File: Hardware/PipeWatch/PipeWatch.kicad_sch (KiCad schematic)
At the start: 19 parts, among them J1 WJ126V-5.0-2P, J3 UART, J4 JTAG, U1 IRM-10-5_C20618064, U3 ESP32-S3-WROOM-1-N16R8, U5 XIAO-ESP32-S3-DIP

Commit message: tweeked the Layout
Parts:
- removed C4: 10n, Capacitor_SMD:C_0603_1608Metric, symbol Device:C
- removed R8: R_Photo, OptoDevice:R_LDR_5.0x4.1mm_P3mm_Vertical, symbol Device:R_Photo
- removed R9: 10M, Resistor_SMD:R_0603_1608Metric, symbol Device:R
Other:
- added sheet PhotowiederstandInnen (Photowiederstand.kicad_sch)

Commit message: Started implementing the accelerometer
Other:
- added sheet MSU (MSU.kicad_sch)
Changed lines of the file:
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@@
+	)
+	(sheet
+		(at 55.88 143.51)
+		(size 12.7 8.89)
+		(exclude_from_sim no)
+		(in_bom yes)
+		(on_board yes)
+		(dnp no)
+		(fields_autoplaced yes)
+		(stroke
+			(width 0.1524)
+			(type solid)
+		)
+		(fill
+			(color 0 0 0 0.0000)
+		)
+		(property "Sheetname" "MSU"
+			(at 55.88 142.7984 0)
+			(effects
+				(font
+					(size 1.27 1.27)
+				)
+				(justify left bottom)
+			)
+		)
+		(property "Sheetfile" "MSU.kicad_sch"
+			(at 55.88 152.9846 0)
+			(effects
+				(font
+					(size 1.27 1.27)
+				)
+				(justify left top)
+			)
+		)
+		(instances
+			(project "PipeWatch"
+				(path "/149975cd-655c-40c3-be76-7a7ba16694c7"
+					(page "5")
+				)
+			)
+		)
 	)
 	(sheet

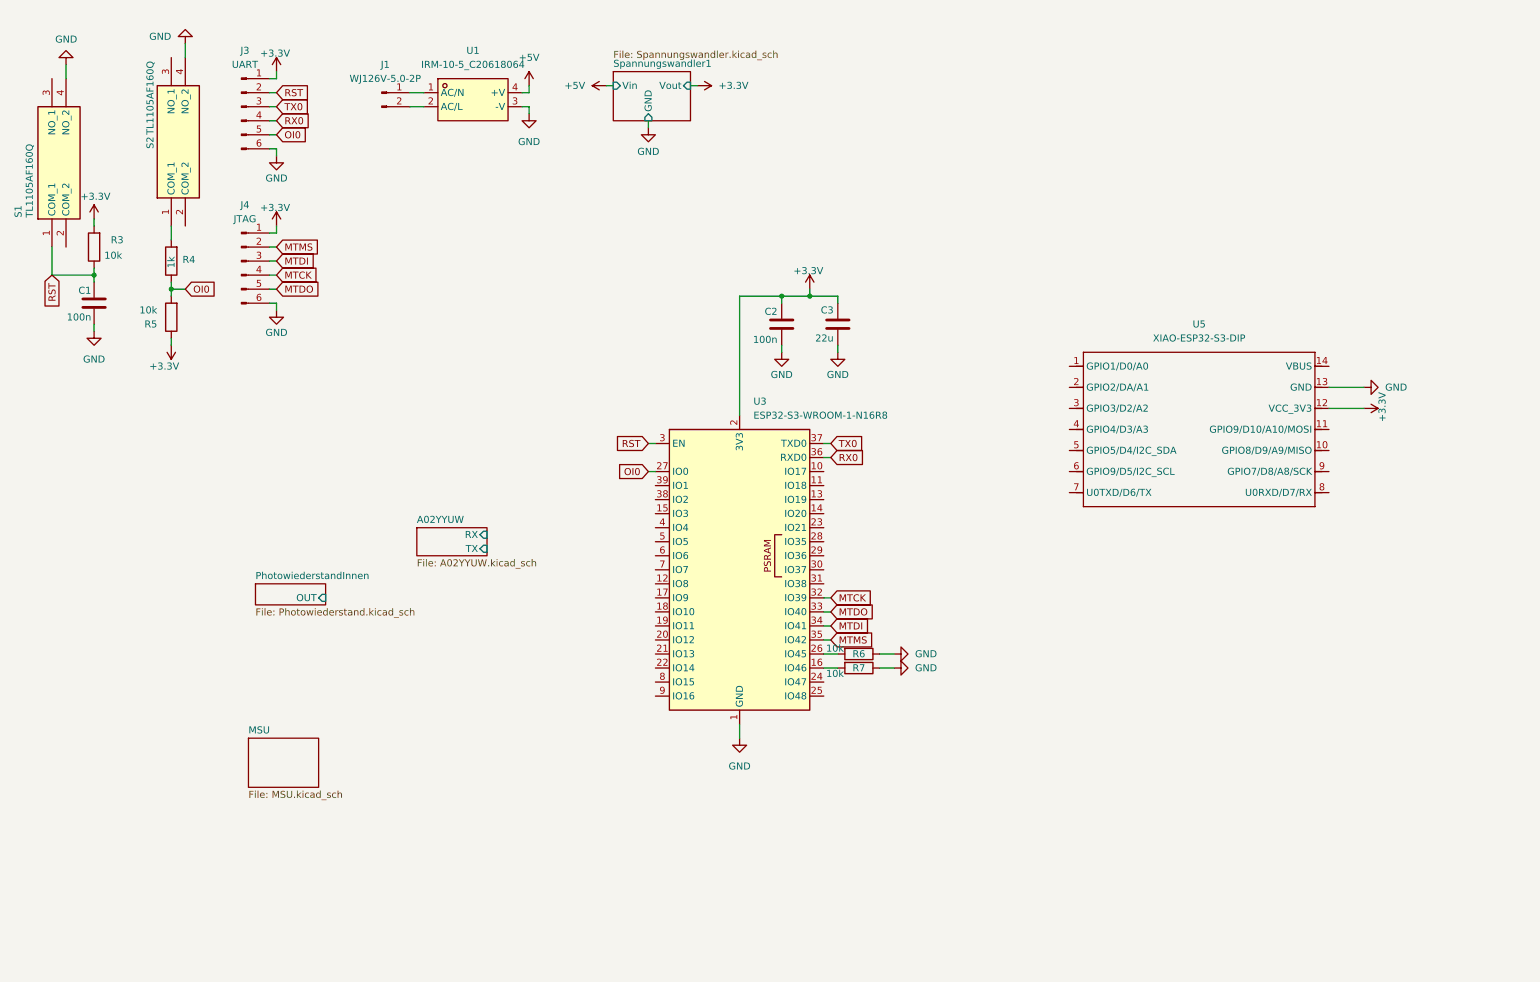
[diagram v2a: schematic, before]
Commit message: added Binky parts and a load of 3d references
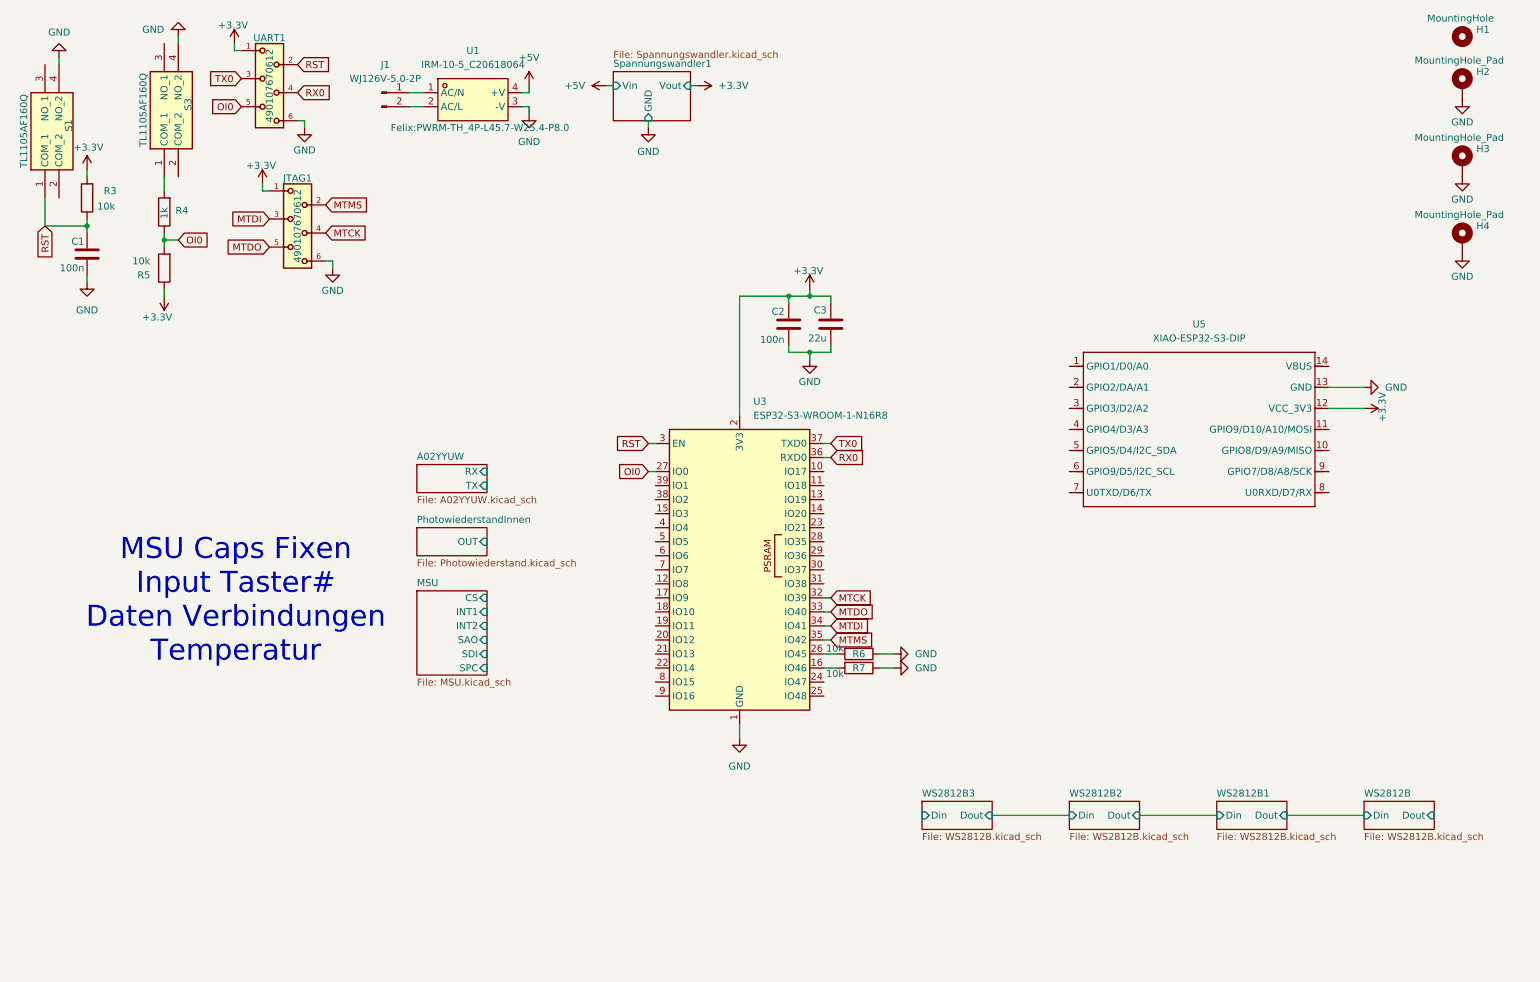
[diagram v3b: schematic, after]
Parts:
- removed J3: UART, Felix_ProgHeader:490107670612, symbol Connector:Conn_01x06_Pin
- removed J4: JTAG, Felix_ProgHeader:490107670612, symbol Connector:Conn_01x06_Pin
- removed S1, S2: TL1105AF160Q, Library:TL1105AF160Q, symbol TL1105AF160Q:TL1105AF160Q
- added H1: MountingHole, MountingHole:MountingHole_3.2mm_M3, symbol Mechanical:MountingHole
- added H2, H3, H4: MountingHole_Pad, MountingHole:MountingHole_3.2mm_M3_DIN965_Pad_TopBottom, symbol Mechanical:MountingHole_Pad
- added JTAG1, UART1: 490107670612, Felix_Connectors:490107670612, symbol Felix_Connectors:490107670612
- added S1, S3: TL1105AF160Q, Felix:TL1105AF160Q, symbol Felix:TL1105AF160Q
- J1: footprint Felix:CONN-TH_WJ126V-5.0-2P -> Felix_Connectors:CONN-TH_WJ126V-5.0-2P
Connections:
- net +3.3V: now also JTAG1.1, UART1.1
- net GND: now also H2.1, H3.1, H4.1, JTAG1.6, S1.4 (NO_2), S3.4 (NO_2), UART1.6
- net MTCK: now also JTAG1.4
- net MTDI: now also JTAG1.3
- net MTDO: now also JTAG1.5
- net MTMS: now also JTAG1.2
- net OI0: now also UART1.5
- net RST: now also S1.1 (COM_1), UART1.2
- net RX0: now also UART1.4
- net TX0: now also UART1.3
- net at R4.2: now also S3.1 (COM_1)
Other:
- added sheet WS2812B (WS2812B.kicad_sch)
- added sheet WS2812B1 (WS2812B.kicad_sch)
- added sheet WS2812B2 (WS2812B.kicad_sch)
- added sheet WS2812B3 (WS2812B.kicad_sch)
- sheet MSU ports: added CS, INT1, INT2, SAO, SDI, SPC; removed none
- note added: "MSU Caps Fixen Input Taster# Daten Verbindungen Temperatur"
- moved on the sheet: C1, C2, C3, R3, R4, R5

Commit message: some changes
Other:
- added sheet Taster (Taster.kicad_sch)
- note added: "Input Taster# Daten Verbindungen Temperatur"
- note removed: "MSU Caps Fixen Input Taster# Daten Verbindungen Temperatur"
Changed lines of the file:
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@@
 	(generator_version "9.0")
 	(paper "A4")
-	(text "MSU Caps Fixen\nInput Taster#\nDaten Verbindungen\nTemperatur\n\n\n"
+	(text "Input Taster#\nDaten Verbindungen\nTemperatur"
 		(exclude_from_sim no)
 		(at 53.594 124.714 0)
@@
 				)
 			)
+		)
+	)
+	(sheet
+		(at 86.36 135.89)
+		(size 12.7 5.08)
+		(exclude_from_sim no)
+		(in_bom yes)
+		(on_board yes)
+		(dnp no)
+		(fields_autoplaced yes)
+		(stroke
+			(width 0.1524)
+			(type solid)
+		)
+		(fill
+			(color 0 0 0 0.0000)
+		)
+		(property "Sheetname" "Taster"
+			(at 86.36 135.1784 0)
+			(effects
+				(font
+					(size 1.27 1.27)
+				)
+				(justify left bottom)
+			)
+		)
+		(property "Sheetfile" "Taster.kicad_sch"
+			(at 86.36 141.5546 0)
+			(effects
+				(font
+					(size 1.27 1.27)
+				)
+				(justify left top)
+			)
+		)
+		(pin "OUT" input
+			(at 99.06 137.16 0)
+			(effects
+				(font
+					(size 1.27 1.27)
+				)
+				(justify right)
+			)
+		)
+		(instances
+			(project "PipeWatch"
+				(path "/149975cd-655c-40c3-be76-7a7ba16694c7"
+					(page "10")
+				)
+			)

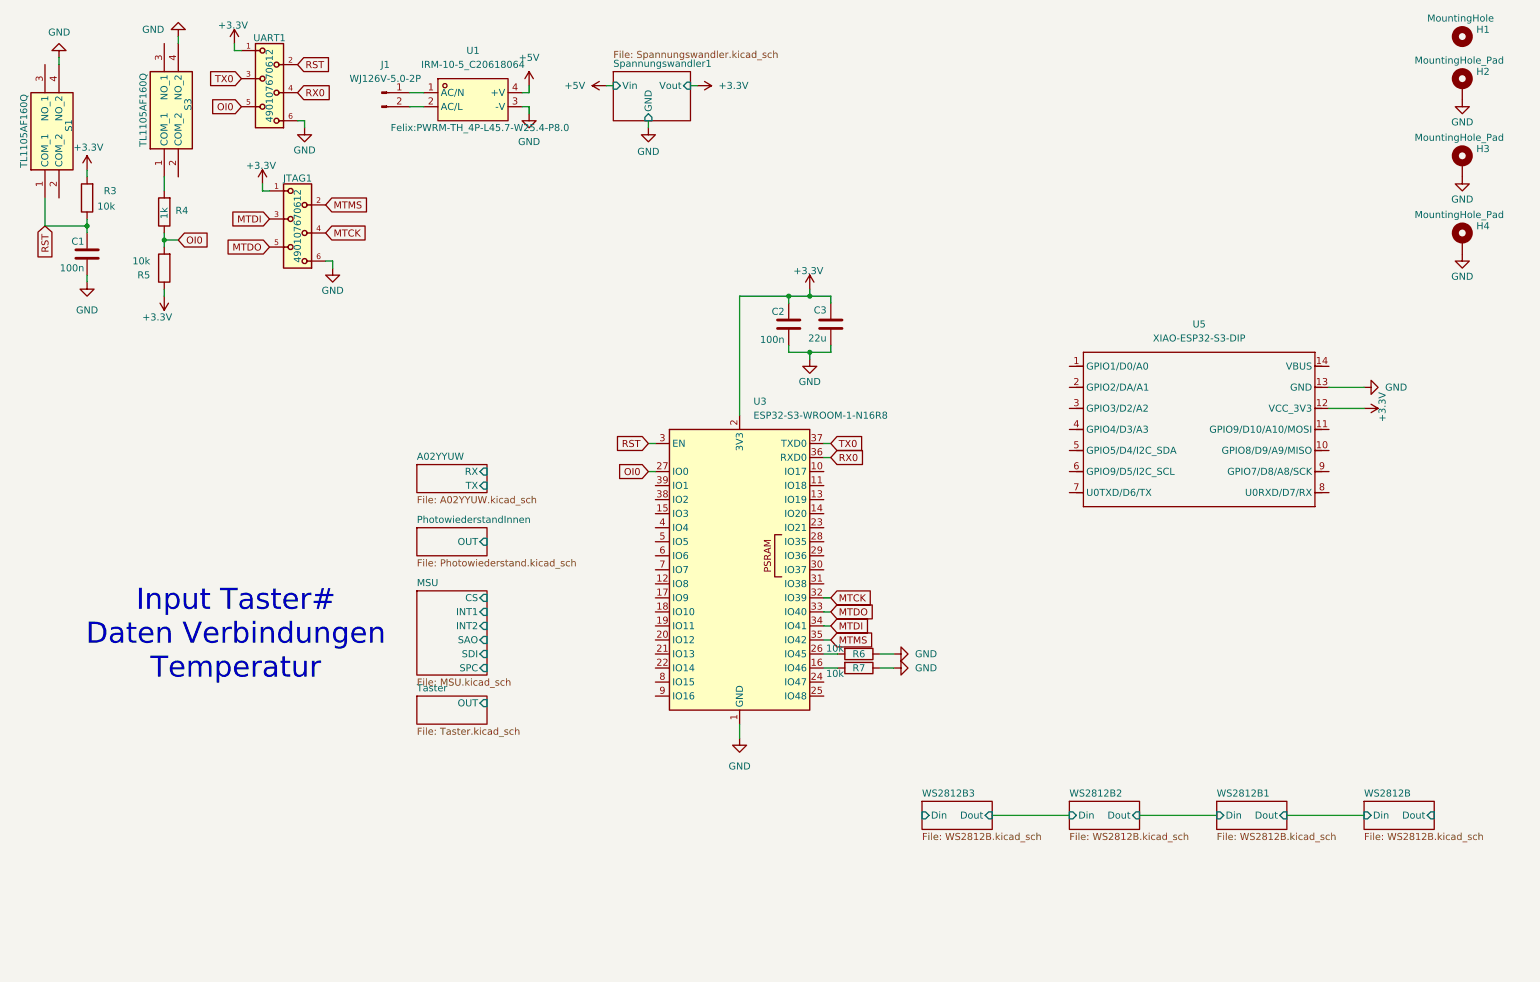
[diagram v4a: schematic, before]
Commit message: Added Ten Sensor
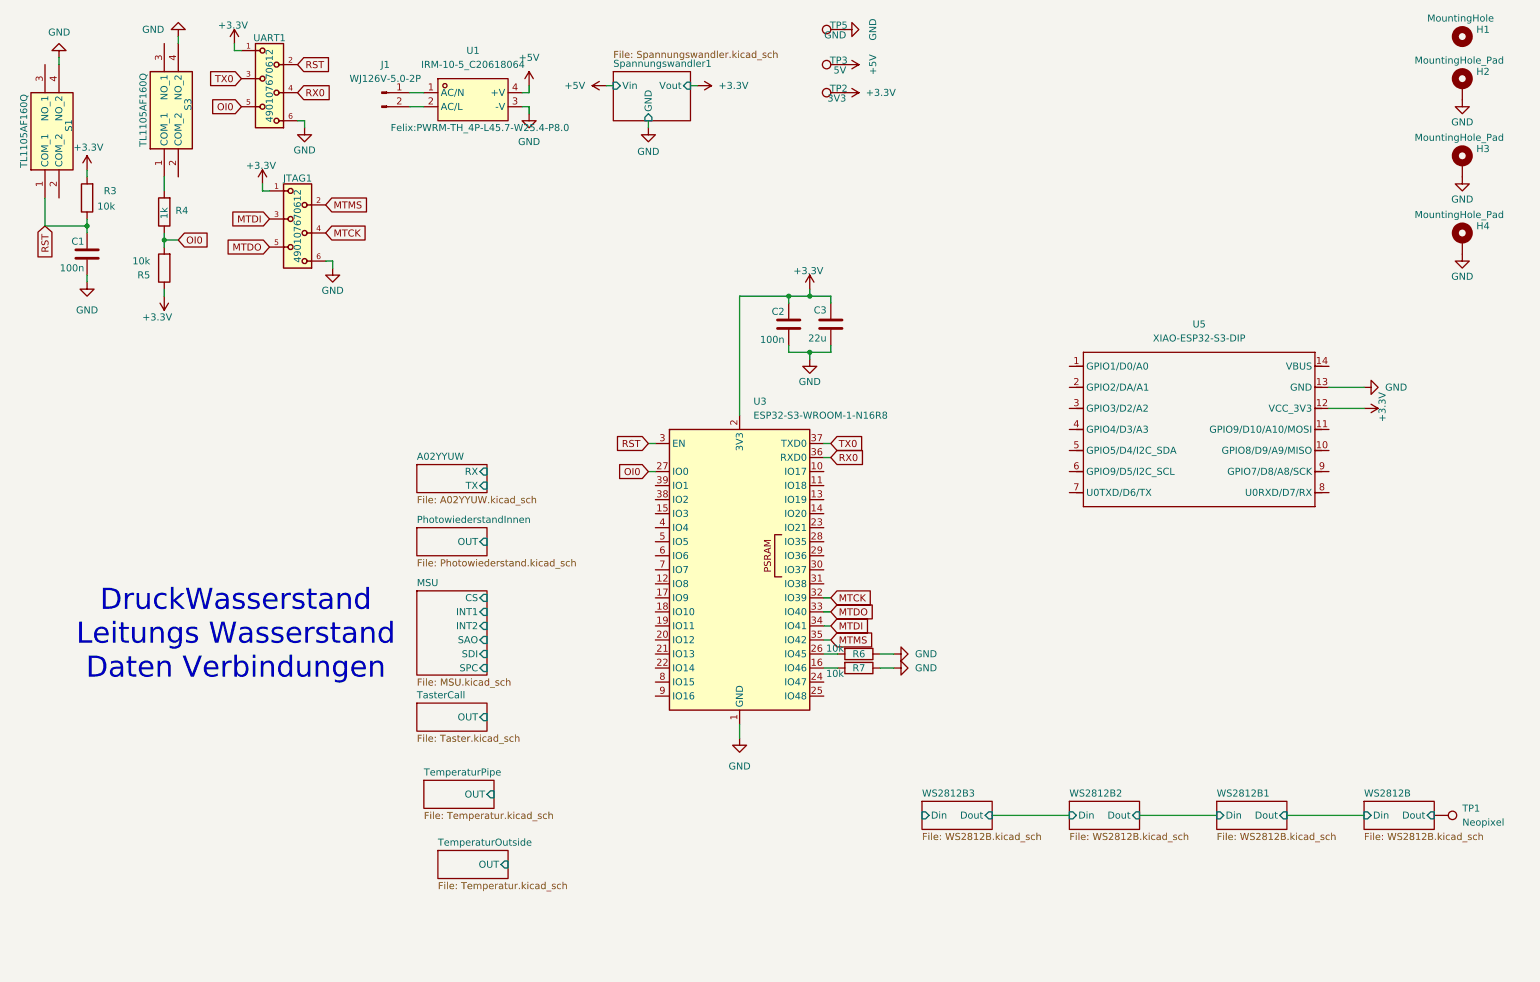
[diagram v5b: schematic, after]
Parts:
- added TP1: Neopixel, TestPoint:TestPoint_Pad_1.0x1.0mm, symbol Connector:TestPoint
- added TP2: 3V3, TestPoint:TestPoint_Pad_2.0x2.0mm, symbol Connector:TestPoint
- added TP3: 5V, TestPoint:TestPoint_Pad_2.0x2.0mm, symbol Connector:TestPoint
- added TP5: GND, TestPoint:TestPoint_Pad_2.0x2.0mm, symbol Connector:TestPoint
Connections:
- net +3.3V: now also TP2.1
- net +5V: now also TP3.1
- net GND: now also TP5.1
- net WS2812B/Dout: now also TP1.1
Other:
- sheet Taster renamed TasterCall
- added sheet TemperaturOutside (Temperatur.kicad_sch)
- added sheet TemperaturPipe (Temperatur.kicad_sch)
- note added: "DruckWasserstand Leitungs Wasserstand Daten Verbindungen"
- note removed: "Input Taster# Daten Verbindungen Temperatur"
